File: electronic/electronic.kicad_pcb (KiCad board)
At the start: 2 copper layers, 68.5 x 75 mm, 24 parts, among them J1 POWER SUPLY, J25 Conn_01x05, J26 Conn_01x04, J27 Conn_01x04, J28 Conn_01x05, J29 Screw_Terminal_01x03, J3 M01, J30 Screw_Terminal_01x03, J4 ENC01, J5 M02, J6 ENC02, J8 M03, J9 ENC03, U1 ESP32-S3-DevKitC

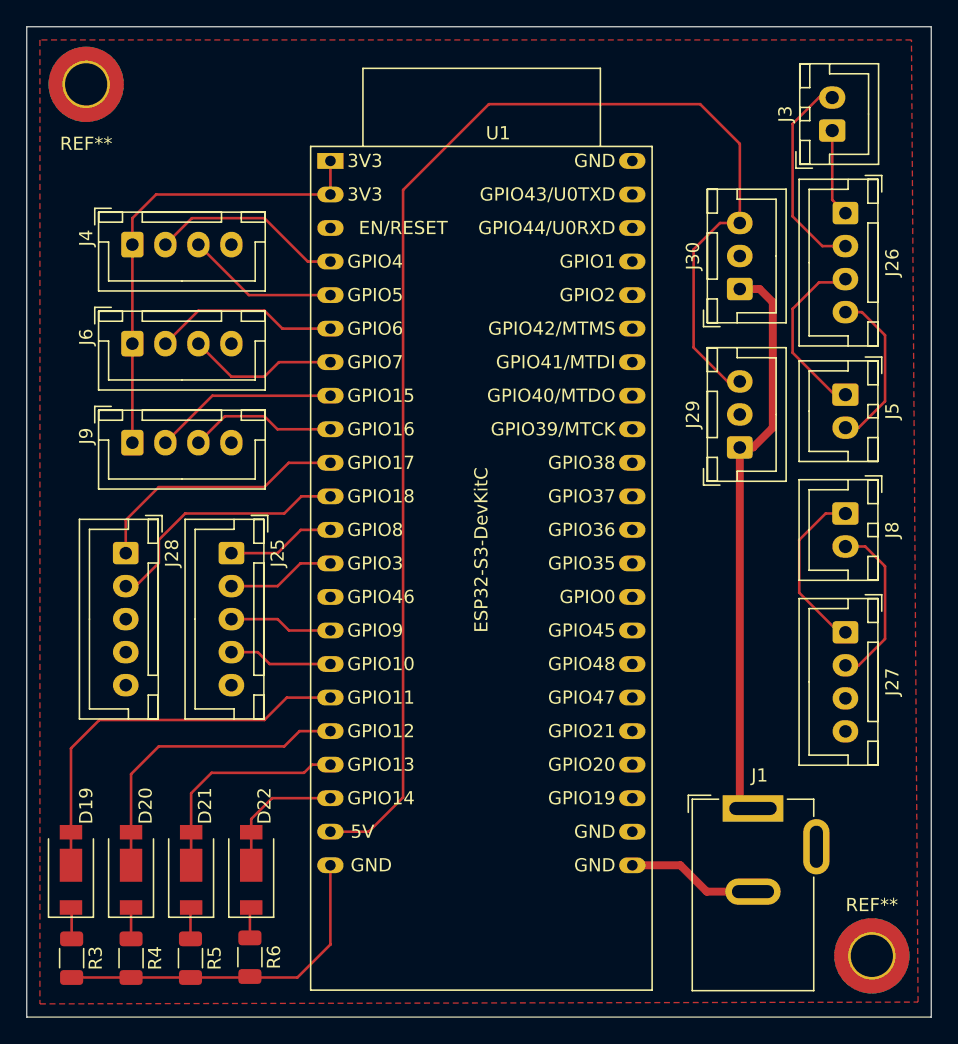
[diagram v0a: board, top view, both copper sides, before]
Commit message: refactor (electronic): update PCB design
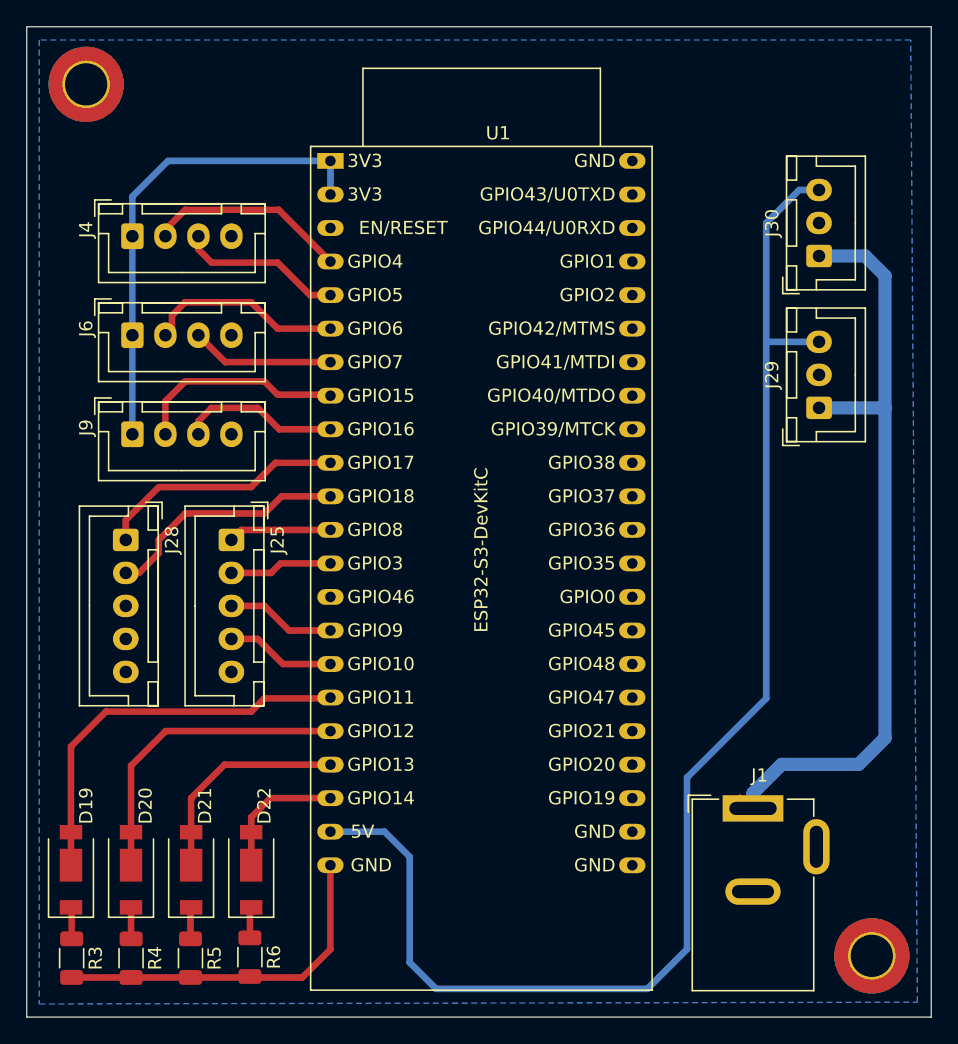
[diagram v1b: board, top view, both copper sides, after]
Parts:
- removed J26, J27: Conn_01x04, Connector_JST:JST_XH_B4B-XH-A_1x04_P2.50mm_Vertical
- removed J3: M01, Connector_JST:JST_XH_B2B-XH-A_1x02_P2.50mm_Vertical
- removed J5: M02, Connector_JST:JST_XH_B2B-XH-A_1x02_P2.50mm_Vertical
- removed J8: M03, Connector_JST:JST_XH_B2B-XH-A_1x02_P2.50mm_Vertical
- moved J29 6.71 mm to (74.0, 43.0)
- moved J30 6.50 mm to (74.0, 31.5)
- moved J25 1.00 mm to (29.5, 53.0)
- moved J28 1.00 mm to (21.5, 53.0)
- moved J4 0.64 mm to (22.0, 30.0)
- moved J6 0.64 mm to (22.0, 37.5)
- moved J9 0.64 mm to (22.0, 45.0)
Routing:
- net +12V: track 43.3 -> 59.9 mm
- net DRVO201: track 15.8 -> 0.00 mm
- net DRVO301: track 13.6 -> 0.00 mm
- net DRVO102: track 13.1 -> 0.00 mm
- net DRVO202: track 12.9 -> 0.00 mm
- net DRVO401: track 12.6 -> 0.00 mm
- net Earth: track 36.6 -> 26.8 mm
- net DRVO101: track 6.66 -> 0.00 mm
- net PH_A03: track 14.0 -> 16.1 mm
- net +3.3V: track 35.3 -> 36.7 mm
- net DRVI102: track 19.8 -> 18.8 mm
- net DRVI202: track 19.3 -> 18.5 mm
- net PH_B01: track 11.6 -> 12.4 mm
- net PH_B03: track 11.2 -> 12.1 mm
- net PH_A02: track 14.1 -> 14.9 mm
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- added copper zone on B.Cu, net Earth
- removed copper zone on F.Cu, net Earth
